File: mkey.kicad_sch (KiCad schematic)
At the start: 159 parts, among them J1 USB_C_REP_2.0, SW1 SW_Push, SW2 SW_Push, U1 ESP32-S3-WROOM-1, U5 SY8088

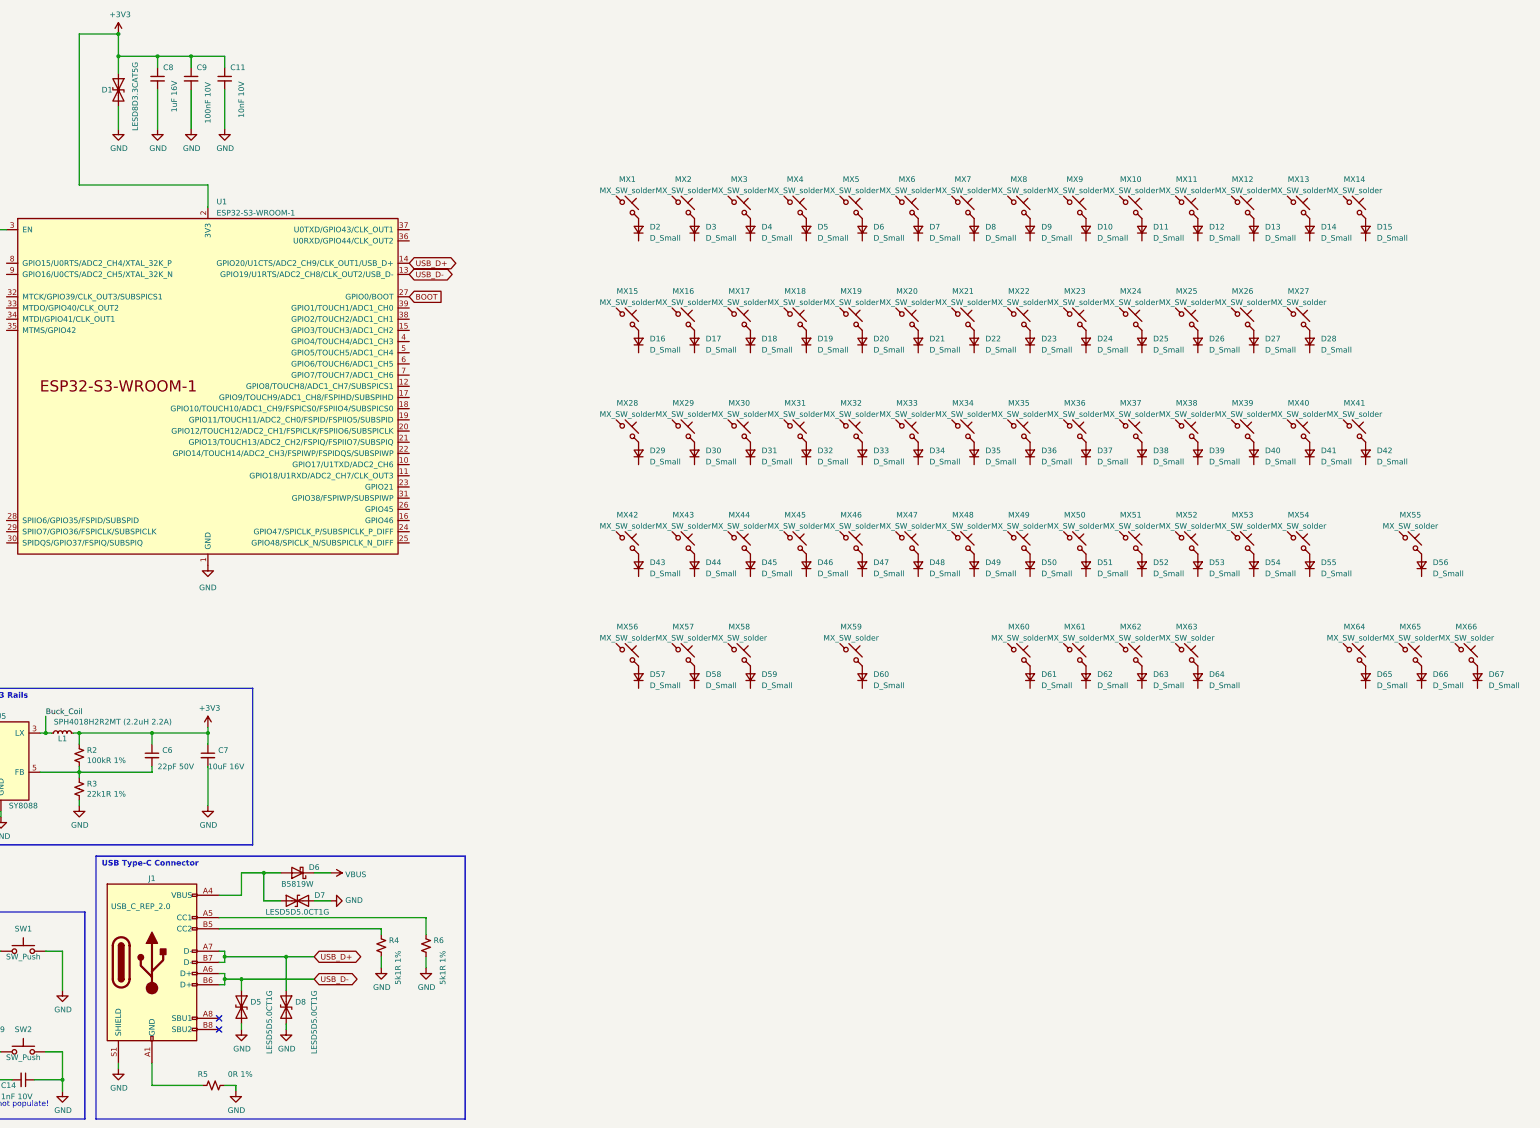
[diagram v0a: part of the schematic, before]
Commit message: Initial KLE import of layout, need to add stabs and other sized keys
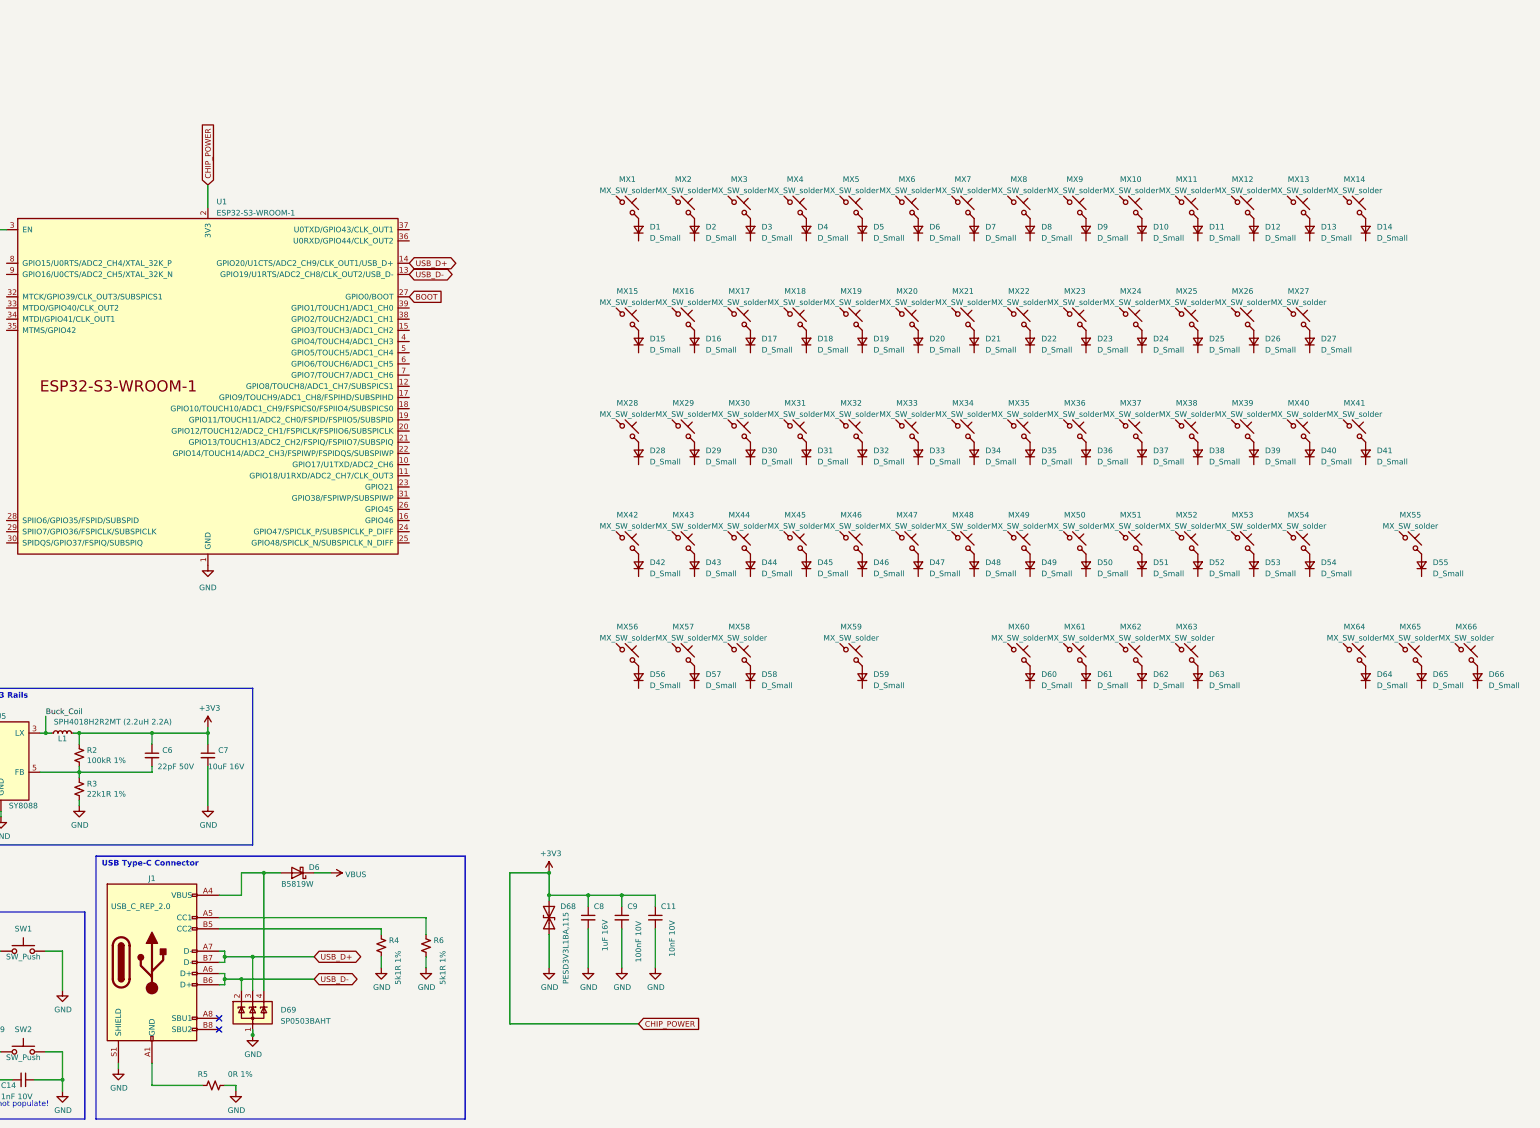
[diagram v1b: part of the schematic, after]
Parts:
- removed D1: LESD8D3.3CAT5G, Rust_Board:SOD-882, symbol Device:D_TVS
- removed D5, D7, D8: LESD5D5.0CT1G, Diode_SMD:D_SOD-523, symbol Device:D_TVS
- added D68: PESD3V3L1BA,115, Diode_SMD:D_SOD-323, symbol Diode:SD05_SOD323
- added D69: SP0503BAHT, Package_TO_SOT_SMD:SOT-143, symbol Power_Protection:SP0503BAHT
- SW2: footprint Connector_USB:USB_C_Receptacle_HRO_TYPE-C-31-M-12 -> Button_Switch_SMD:SW_SPST_PTS810
- renumbered D2 to D1, D11 to D10, D12 to D11, D13 to D12, D14 to D13, D15 to D14, D16 to D15, D17 to D16, D18 to D17, D19 to D18, D20 to D19, D3 to D2, D21 to D20, D22 to D21, D23 to D22, D24 to D23, D25 to D24, D26 to D25, D27 to D26, D28 to D27, D29 to D28, D30 to D29, D4 to D3, D31 to D30, D32 to D31, D33 to D32, D34 to D33, D35 to D34, D36 to D35, D37 to D36, D38 to D37, D39 to D38, D40 to D39, D5 to D4, D41 to D40, D42 to D41, D43 to D42, D44 to D43, D45 to D44, D46 to D45, D47 to D46, D48 to D47, D49 to D48, D50 to D49, D6 to D5, D51 to D50, D52 to D51, D53 to D52, D54 to D53, D55 to D54, D56 to D55, D57 to D56, D58 to D57, D59 to D58, D60 to D59, D7 to D6, D61 to D60, D62 to D61, D63 to D62, D64 to D63, D65 to D64, D66 to D65, D67 to D66, D8 to D7, D9 to D8, D10 to D9
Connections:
- net +3V3: now also D68.2 (A2)
- net GND: now also D68.1 (A1), D69.1 (A)
- net USB_D+: now also D69.3 (K)
- net USB_D-: now also D69.2 (K)
- net at D6.2 (A), J1.A4 (VBUS), J1.A9 (VBUS)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: now also D69.4 (K)

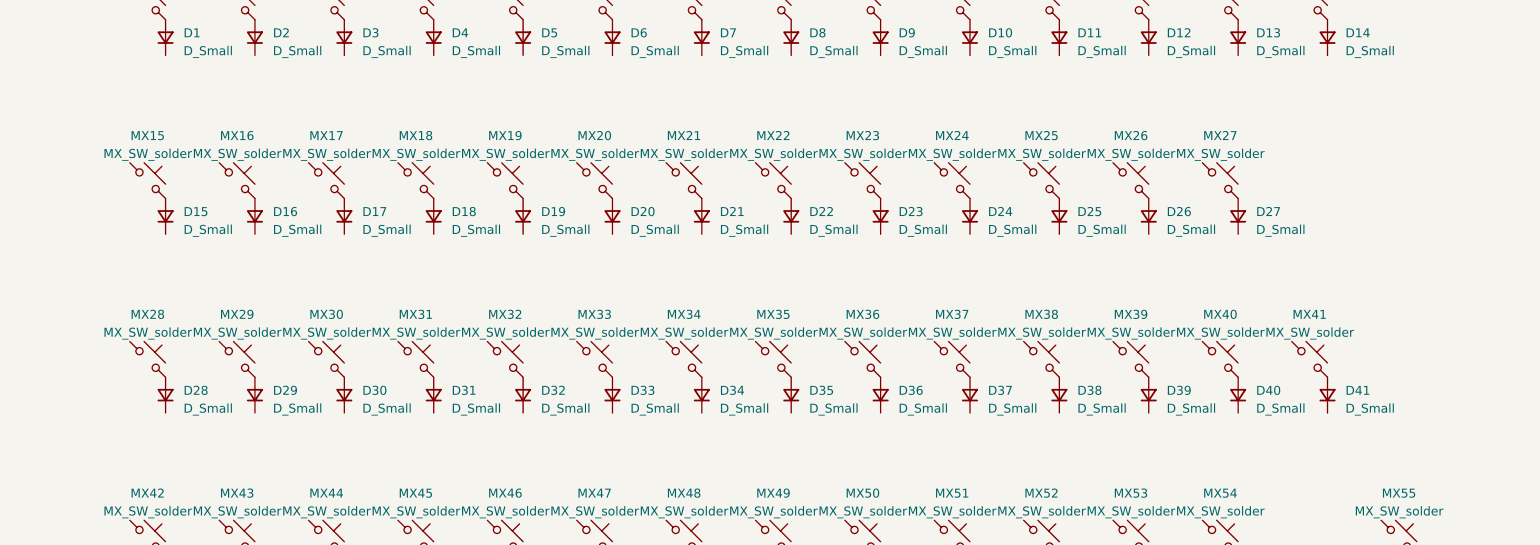
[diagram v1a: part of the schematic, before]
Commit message: flipped diodes and smd's to back layer
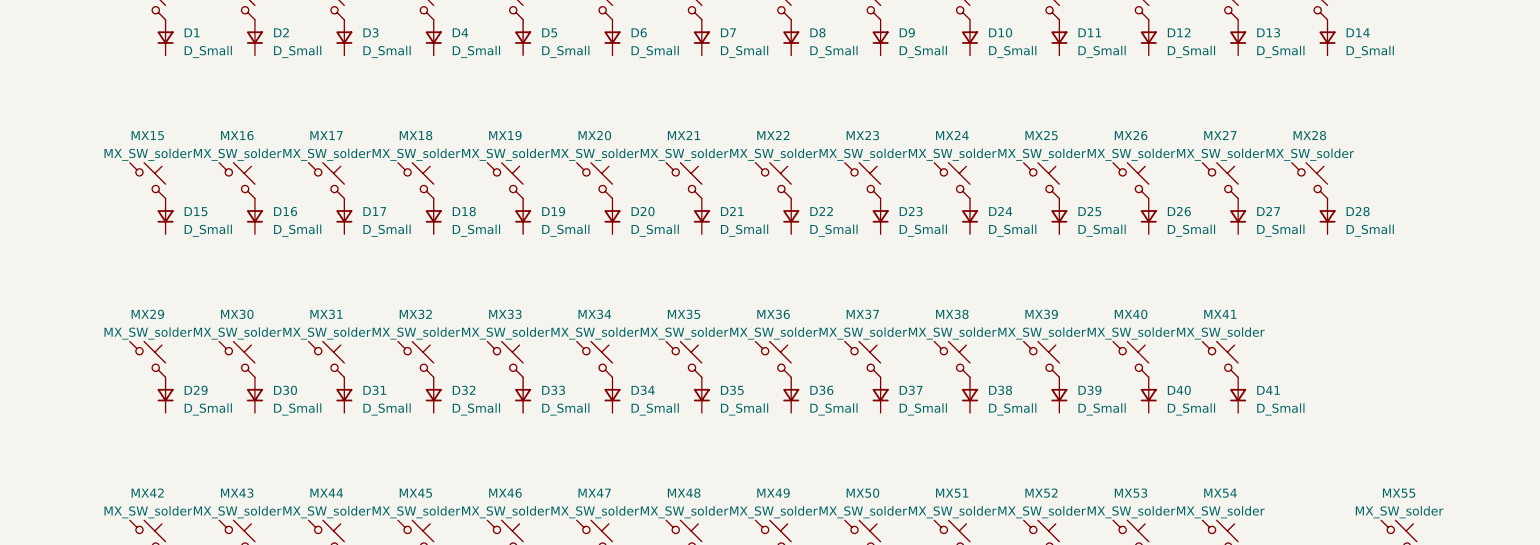
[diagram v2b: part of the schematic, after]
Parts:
- MX15: footprint PCM_marbastlib-mx:SW_MX_1u -> PCM_marbastlib-mx:SW_MX_1.5u
- MX29: footprint PCM_marbastlib-mx:SW_MX_1u -> PCM_marbastlib-mx:SW_MX_1.75u
- MX42, MX56, MX57, MX58, MX60, MX61, MX62, MX63: footprint PCM_marbastlib-mx:SW_MX_1u -> PCM_marbastlib-mx:SW_MX_1.25u
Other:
- moved on the sheet: D28, D29, D30, D31, D32, D33, D34, D35, D36, D37, D38, D39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

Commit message: Added stabs
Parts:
- added S1: MX_stab, PCM_marbastlib-mx:STAB_MX_P_6.25u, symbol PCM_marbastlib-mx:MX_stab
- added S2: MX_stab, PCM_marbastlib-mx:STAB_MX_P_2u, symbol PCM_marbastlib-mx:MX_stab
- added S4: MX_stab, PCM_marbastlib-mx:STAB_MX_P_2.75u, symbol PCM_marbastlib-mx:MX_stab
- added S5: MX_stab, PCM_marbastlib-mx:STAB_MX_ISO-ROT, symbol PCM_marbastlib-mx:MX_stab
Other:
- moved on the sheet: D55, D64, D65, D66, MX55, MX64, MX65, MX66

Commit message: switch out small comps, to 0603's, start draft routing
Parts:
- C10, C11, C14, C8, C9: footprint Capacitor_SMD:C_0402_1005Metric -> Capacitor_SMD:C_0603_1608Metric
- R1, R19, R2, R3, R4, R5, R6, R8: footprint Resistor_SMD:R_0402_1005Metric -> Resistor_SMD:R_0603_1608Metric
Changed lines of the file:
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@@
       (effects (font (size 1.27 1.27)) (justify left))
     )
-    (property "Footprint" "Resistor_SMD:R_0402_1005Metric" (at 34.29 62.23 0)
+    (property "Footprint" "Resistor_SMD:R_0603_1608Metric" (at 34.29 62.23 0)
       (effects (font (size 1.27 1.27)) hide)
     )
@@
       (effects (font (size 1.27 1.27)) (justify left))
     )
-    (property "Footprint" "Capacitor_SMD:C_0402_1005Metric" (at 34.29 73.66 0)
+    (property "Footprint" "Capacitor_SMD:C_0603_1608Metric" (at 34.29 73.66 0)
       (effects (font (size 1.27 1.27)) hide)
     )
@@
       (effects (font (size 1.27 1.27)) (justify left))
     )
-    (property "Footprint" "Capacitor_SMD:C_0402_1005Metric" (at 189.23 224.79 0)
+    (property "Footprint" "Capacitor_SMD:C_0603_1608Metric" (at 189.23 224.79 0)
       (effects (font (size 1.27 1.27)) hide)
     )
@@
       (effects (font (size 1.27 1.27)) (justify left))
     )
-    (property "Footprint" "Resistor_SMD:R_0402_1005Metric" (at 144.78 231.14 0)
+    (property "Footprint" "Resistor_SMD:R_0603_1608Metric" (at 144.78 231.14 0)
       (effects (font (size 1.27 1.27)) hide)
     )
@@
       (effects (font (size 1.27 1.27)) (justify left))
     )
-    (property "Footprint" "Resistor_SMD:R_0402_1005Metric" (at 96.52 262.89 0)
+    (property "Footprint" "Resistor_SMD:R_0603_1608Metric" (at 96.52 262.89 0)
       (effects (font (size 1.27 1.27)) hide)
     )
@@
       (effects (font (size 1.27 1.27)) (justify left))
     )
-    (property "Footprint" "Resistor_SMD:R_0402_1005Metric" (at 66.04 195.58 0)
+    (property "Footprint" "Resistor_SMD:R_0603_1608Metric" (at 66.04 195.58 0)
       (effects (font (size 1.27 1.27)) hide)
     )
@@
       (effects (font (size 1.27 1.27)) (justify left))
     )
-    (property "Footprint" "Resistor_SMD:R_0402_1005Metric" (at 34.29 187.96 0)
+    (property "Footprint" "Resistor_SMD:R_0603_1608Metric" (at 34.29 187.96 0)
       (effects (font (size 1.27 1.27)) hide)
     )
@@
       (effects (font (size 1.27 1.27)) (justify left))
     )
-    (property "Footprint" "Capacitor_SMD:C_0402_1005Metric" (at 53.34 261.62 0)
+    (property "Footprint" "Capacitor_SMD:C_0603_1608Metric" (at 53.34 261.62 0)
       (effects (font (size 1.27 1.27)) hide)
     )
@@
       (effects (font (size 1.27 1.27)) (justify left))
     )
-    (property "Footprint" "Capacitor_SMD:C_0402_1005Metric" (at 196.85 224.79 0)
+    (property "Footprint" "Capacitor_SMD:C_0603_1608Metric" (at 196.85 224.79 0)
       (effects (font (size 1.27 1.27)) hide)
     )
@@
       (effects (font (size 1.27 1.27)) (justify left))
     )
-    (property "Footprint" "Resistor_SMD:R_0402_1005Metric" (at 66.04 187.96 0)
+    (property "Footprint" "Resistor_SMD:R_0603_1608Metric" (at 66.04 187.96 0)
       (effects (font (size 1.27 1.27)) hide)
     )
@@
       (effects (font (size 1.27 1.27)) (justify left))
     )
-    (property "Footprint" "Resistor_SMD:R_0402_1005Metric" (at 134.62 231.14 0)
+    (property "Footprint" "Resistor_SMD:R_0603_1608Metric" (at 134.62 231.14 0)
       (effects (font (size 1.27 1.27)) hide)
     )
@@
       (effects (font (size 1.27 1.27)) (justify left))
     )
-    (property "Footprint" "Capacitor_SMD:C_0402_1005Metric" (at 181.61 224.79 0)
+    (property "Footprint" "Capacitor_SMD:C_0603_1608Metric" (at 181.61 224.79 0)
       (effects (font (size 1.27 1.27)) hide)
     )
@@
       (effects (font (size 1.27 1.27)) (justify left))
     )
-    (property "Footprint" "Resistor_SMD:R_0402_1005Metric" (at 44.45 250.19 0)
+    (property "Footprint" "Resistor_SMD:R_0603_1608Metric" (at 44.45 250.19 0)
       (effects (font (size 1.27 1.27)) hide)
     )
